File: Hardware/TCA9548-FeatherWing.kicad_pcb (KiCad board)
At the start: 2 copper layers, 51.5 x 40 mm, 44 parts, among them J1 Conn_01x03, J10 JST_SH, J11 Conn_01x16, J12 Conn_01x12, J2 JST_PH-SH, J3 JST_PH-SH, J4 Conn_01x03, J5 JST_SH, J6 JST_SH, J7 JST_SH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

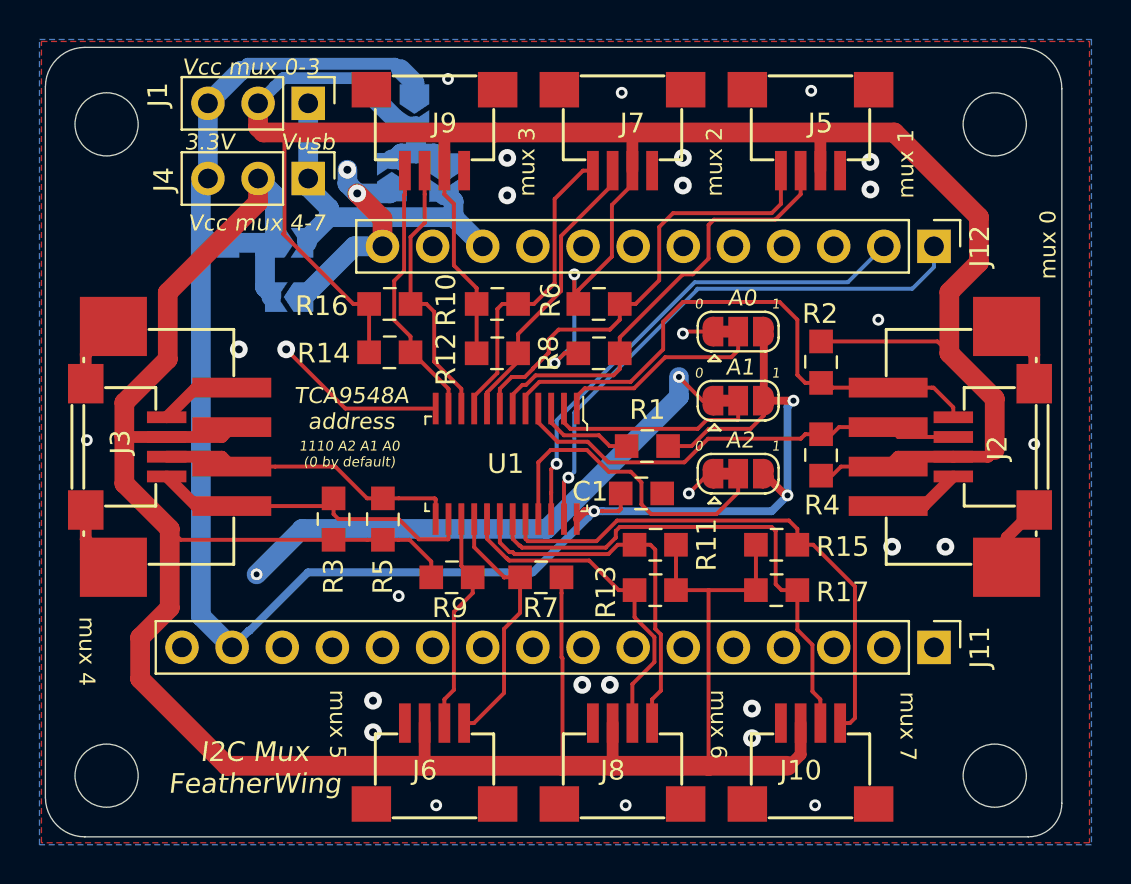
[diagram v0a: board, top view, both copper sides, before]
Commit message: Add pullups to source lines
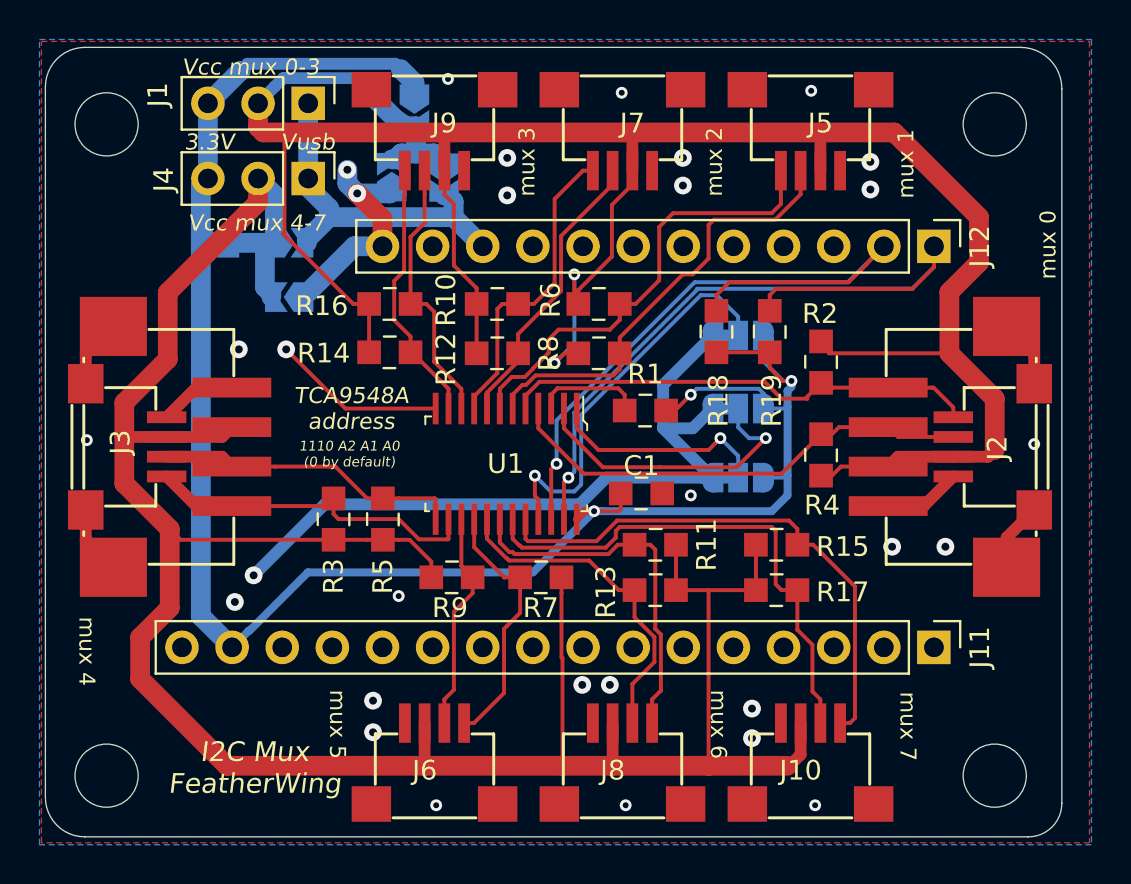
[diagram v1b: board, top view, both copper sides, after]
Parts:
- added R18: 10k, digikey-footprints:0805, F.Cu at (237.9, 47.5)
- added R19: 10k, digikey-footprints:0805, F.Cu at (240.6, 47.5)
- JP1, JP2, JP3: moved to B.Cu
- moved JP1 7.40 mm to (239.0, 54.9)
- moved JP3 7.00 mm to (239.0, 47.7)
- moved R1 1.80 mm to (234.3, 51.5)
- moved JP2 0.40 mm to (239.0, 51.4)
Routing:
- net SDA: track 28.0 -> 38.7 mm
- net SCL: track 25.3 -> 35.7 mm
- net GND: track 62.1 -> 68.7 mm, vias 30 -> 28
- net Net-(J2-Pad4): track 29.5 -> 24.4 mm
- net +3V3: track 93.4 -> 97.8 mm
- net Net-(JP2-Pad2): track 10.8 -> 15.2 mm, vias 0 -> 1
- net Net-(JP3-Pad2): track 16.7 -> 20.5 mm, vias 0 -> 1
- net Net-(J2-Pad3): track 23.0 -> 23.6 mm
- net Net-(JP1-Pad2): track 10.7 -> 11.4 mm, vias 0 -> 1
